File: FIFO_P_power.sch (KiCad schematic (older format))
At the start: 22 parts, among them J4 Jack-DC, J5 Screw_Terminal_01x08, U10 LM2776, U11 LM1117-3.3, U9 LM2940CT-5.0

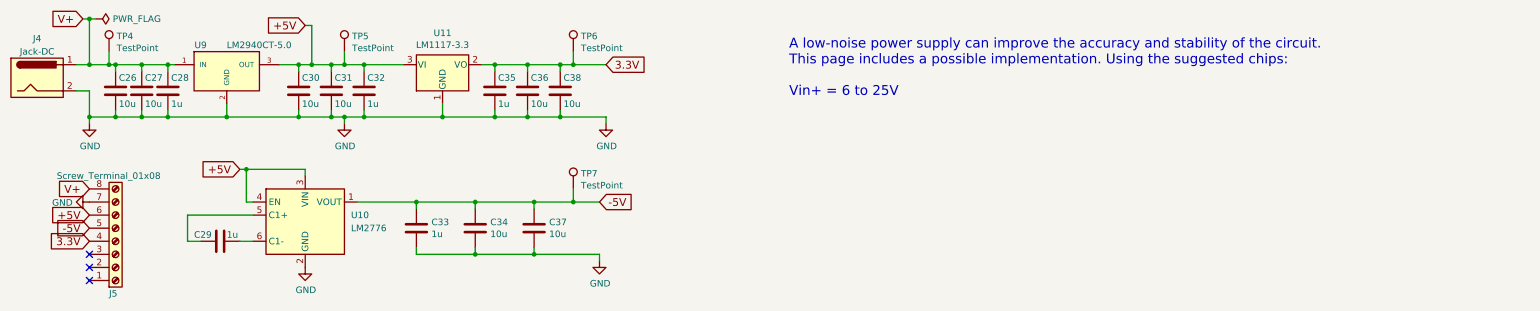
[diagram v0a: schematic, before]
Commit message: Reannotated and replaced many components. Bypass capacitors everywhere.
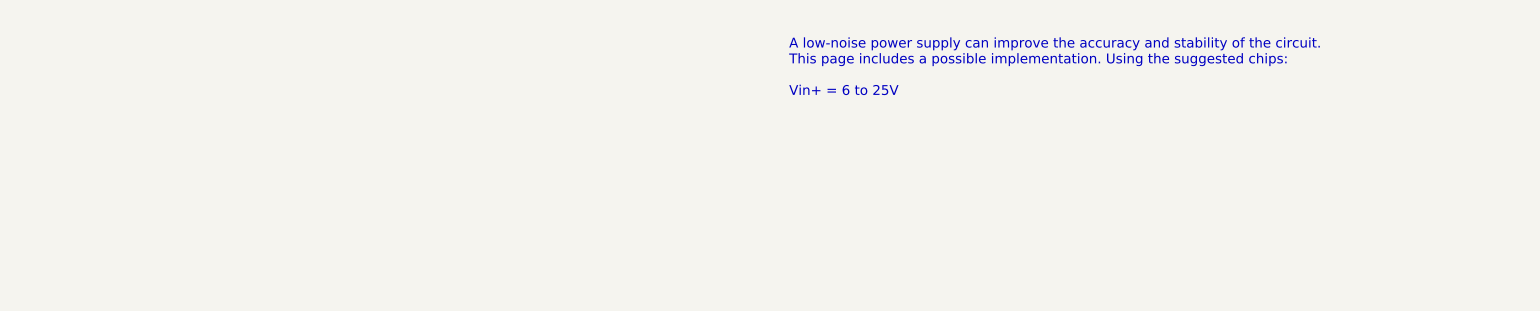
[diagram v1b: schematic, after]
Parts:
- removed C26, C27, C30, C31, C34, C36, C37, C38: 10u, Capacitor_SMD:C_0805_2012Metric_Pad1.15x1.40mm_HandSolder, symbol Device:C
- removed C28, C29, C32, C33, C35: 1u, Capacitor_SMD:C_0805_2012Metric_Pad1.15x1.40mm_HandSolder, symbol Device:C
- removed J4: Jack-DC, Connector_BarrelJack:BarrelJack_Horizontal, symbol Connector:Jack-DC
- removed J5: Screw_Terminal_01x08, TerminalBlock_Phoenix:TerminalBlock_Phoenix_MKDS-3-8-5.08_1x08_P5.08mm_Horizontal, symbol Connector:Screw_Terminal_01x08
- removed TP4, TP5, TP6, TP7: TestPoint, FIFO_P:Test_Pin, symbol Connector:TestPoint
- removed U10: LM2776, Package_TO_SOT_SMD:SOT-23-6, symbol Regulator_SwitchedCapacitor:LM2776
- removed U11: LM1117-3.3, Package_TO_SOT_SMD:TO-252-3_TabPin2, symbol Regulator_Linear:LM1117-3.3
- removed U9: LM2940CT-5.0, Package_TO_SOT_THT:TO-220-3_Horizontal_TabDown, symbol FIFO_P:LM2940CT-5.0
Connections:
- no-connect marks 3 -> 0
